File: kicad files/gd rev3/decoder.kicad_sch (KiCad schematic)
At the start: 32 parts

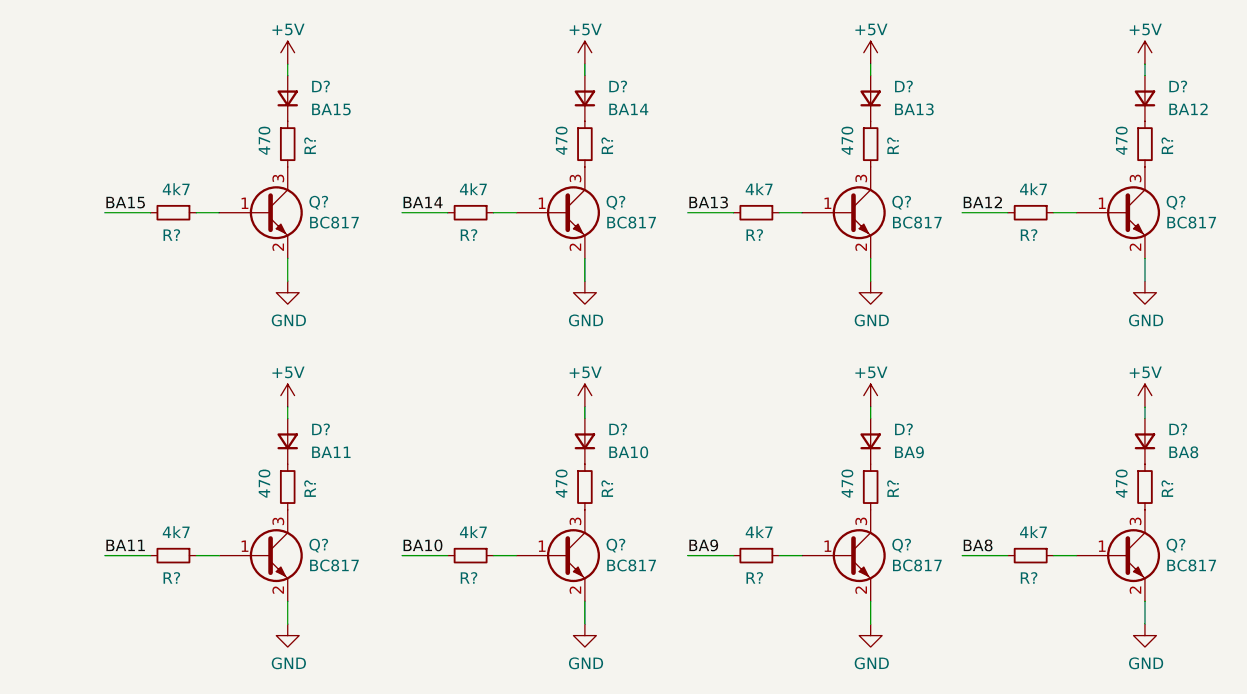
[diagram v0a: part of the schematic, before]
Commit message: started work on kbd2040 section, need to define a lot of IO
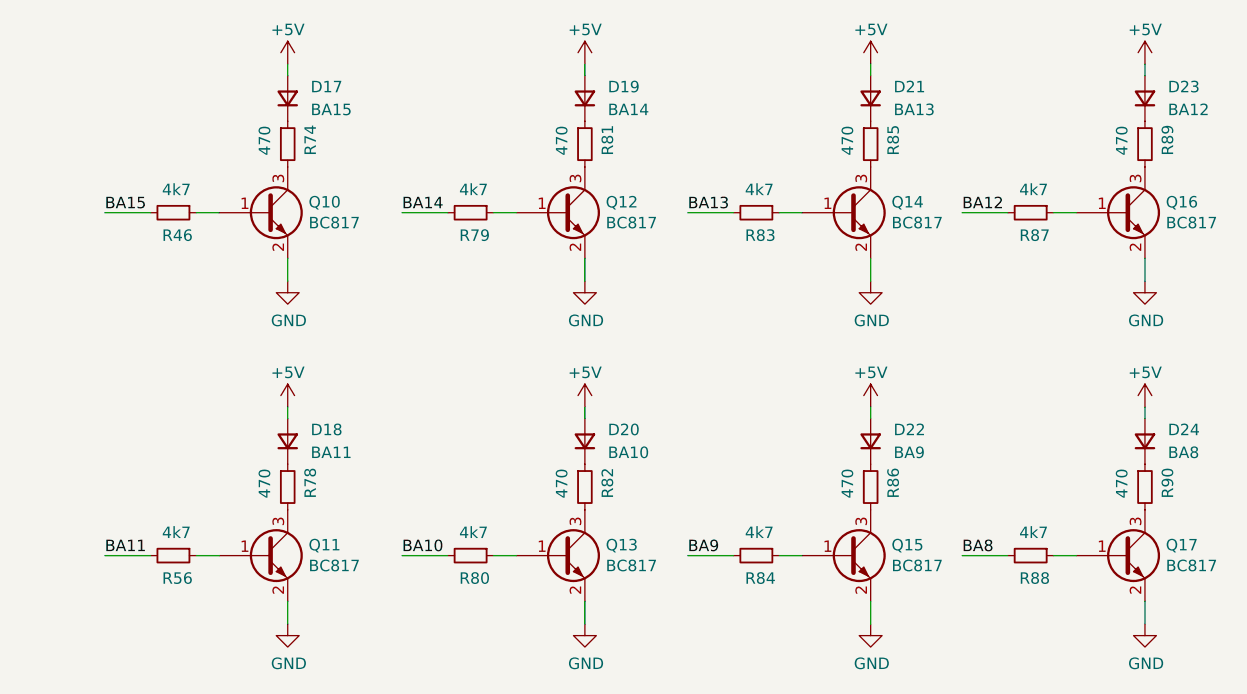
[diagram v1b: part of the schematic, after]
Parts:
- gave numbers to parts that had none: 32

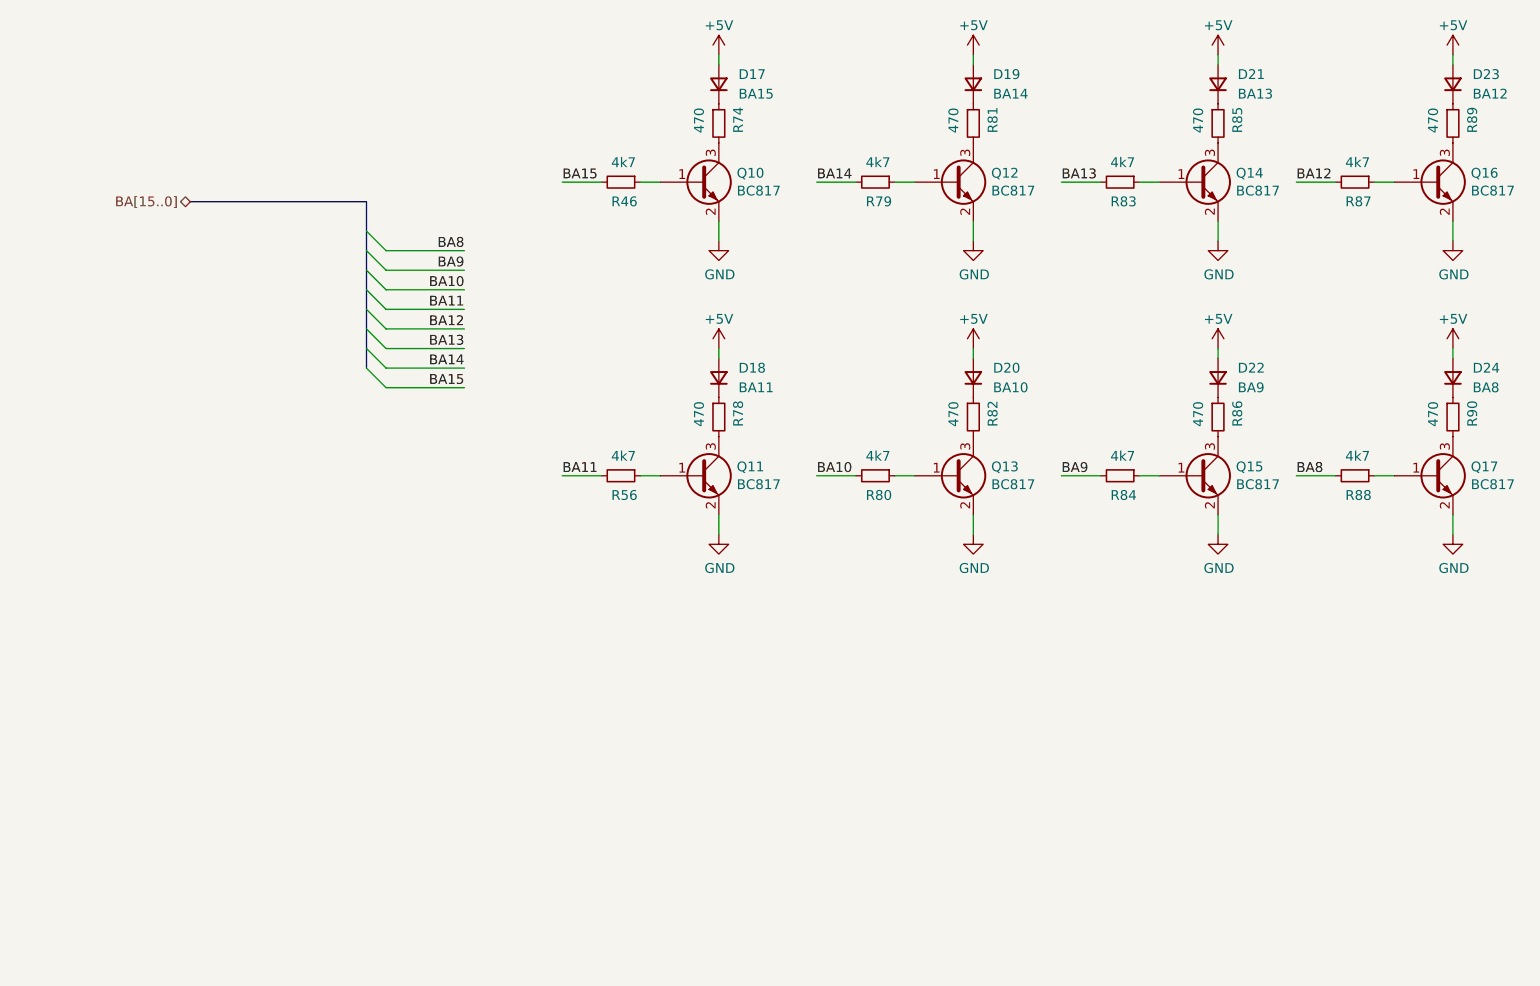
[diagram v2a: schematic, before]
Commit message: added rj-style decoder for upper address display
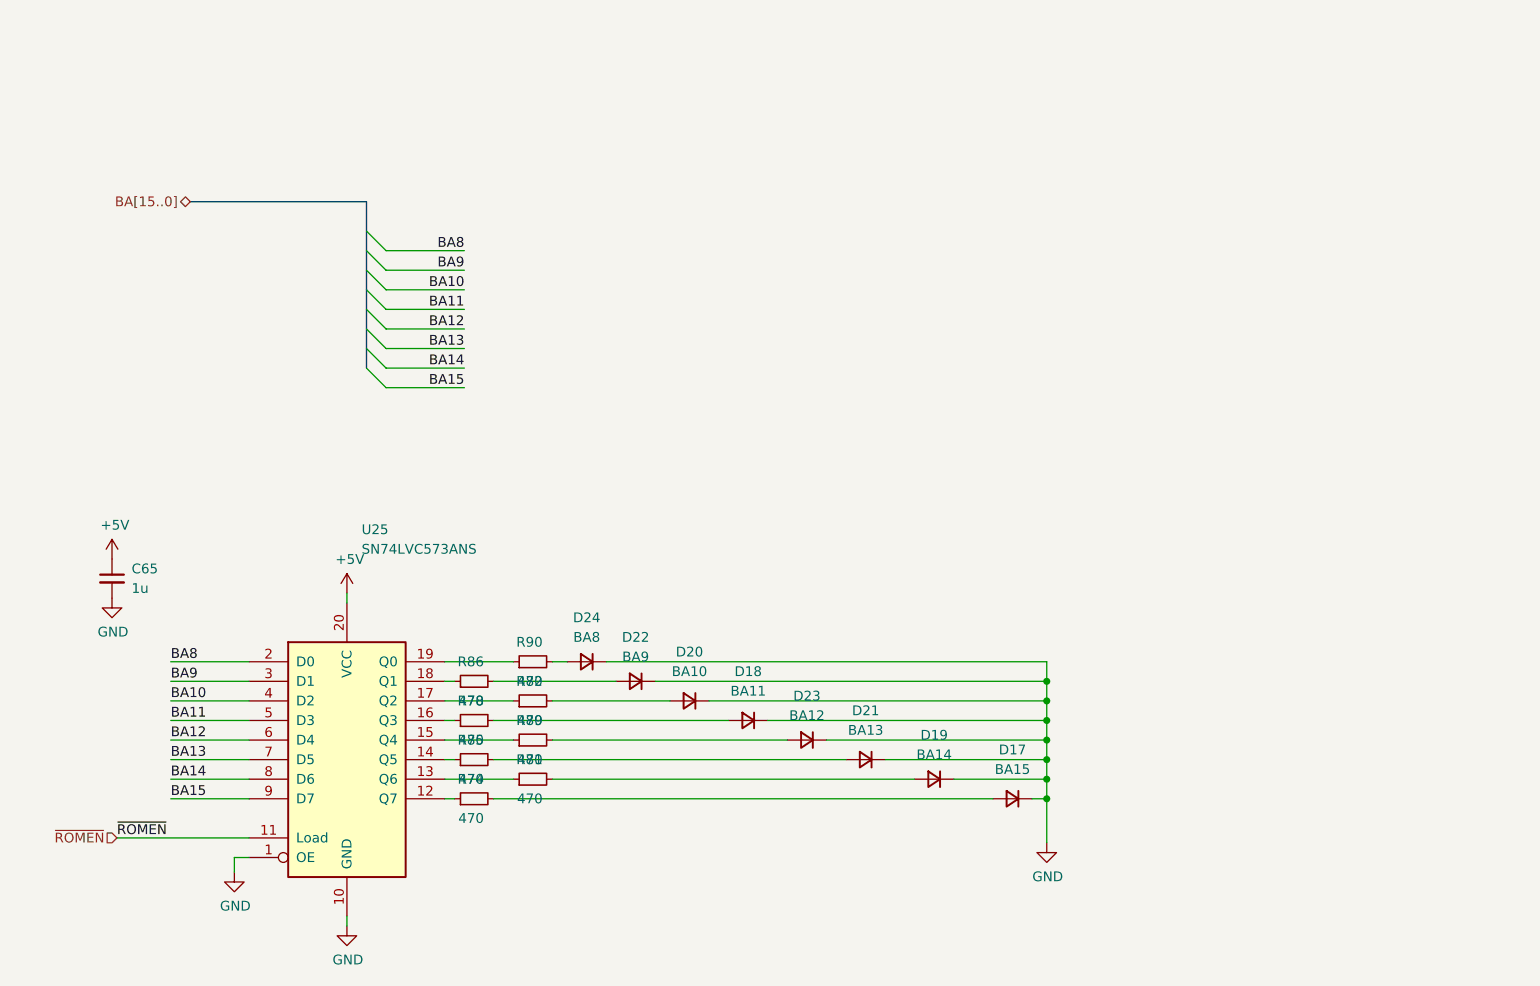
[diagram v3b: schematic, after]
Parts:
- removed Q10, Q11, Q12, Q13, Q14, Q15, Q16, Q17: BC817, Package_TO_SOT_SMD:SOT-23, symbol Device:Q_NPN_BEC
- removed R46, R56, R79, R80, R83, R84, R87, R88: 4k7, Resistor_SMD:R_0805_2012Metric, symbol My_Library:R_0805
- added C65: 1u, Capacitor_SMD:C_0603_1608Metric, symbol Device:C_Small
- added U25: SN74LVC573ANS, Package_SO:SO-20_5.3x12.6mm_P1.27mm, symbol 74xx:74LS573
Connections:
- net +5V: now also C65.1, U25.20 (VCC); no longer D17.2 (A), D18.2 (A), D19.2 (A), D20.2 (A), D21.2 (A), D22.2 (A), D23.2 (A), D24.2 (A)
- net BA10: now also U25.4 (D2)
- net BA11: now also U25.5 (D3)
- net BA12: now also U25.6 (D4)
- net BA13: now also U25.7 (D5)
- net BA14: now also U25.8 (D6)
- net BA15: now also U25.9 (D7)
- net BA8: now also U25.2 (D0)
- net BA9: now also U25.3 (D1)
- net GND: now also D17.1 (K), D18.1 (K), D19.1 (K), D20.1 (K), D21.1 (K), D22.1 (K), D23.1 (K), D24.1 (K), C65.2, U25.1 (OE), U25.10 (GND)
- net at R85.1: now also U25.14 (Q5); no longer D21.1 (K)
- net at R85.2: now also D21.2 (A)
- net at R82.2: now also D20.2 (A)
- net at R74.2: now also D17.2 (A)
- net at R74.1: now also U25.12 (Q7); no longer D17.1 (K)
- net at R89.2: now also D23.2 (A)
- net at R86.2: now also D22.2 (A)
- net at R78.1: now also U25.16 (Q3); no longer D18.1 (K)
- net at R78.2: now also D18.2 (A)
- net at R82.1: now also U25.17 (Q2); no longer D20.1 (K)
- net at R90.1: now also U25.19 (Q0); no longer D24.1 (K)
- net at R86.1: now also U25.18 (Q1); no longer D22.1 (K)
- net at R89.1: now also U25.15 (Q4); no longer D23.1 (K)
- net at R90.2: now also D24.2 (A)
- net at R81.2: now also D19.2 (A)
- net at R81.1: now also U25.13 (Q6); no longer D19.1 (K)
- new net ~{ROMEN}: U25.11 (Load)
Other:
- moved on the sheet: D17, D18, D19, D20, D21, D22, D23, D24, R74, R78, R81, R82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

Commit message: Rev 3b, after first fab messed up boards.
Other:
- company: (none) -> twitch.tv/baldengineer
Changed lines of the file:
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@@
 (kicad_sch (version 20211123) (generator eeschema)
   (paper "A4")
+  (title_block
+    (date "2022-06-27")
+    (rev "3b")
+    (company "twitch.tv/baldengineer")
+  )
   (junction (at 158.115 123.19) (diameter 0) (color 0 0 0 0)
   )
